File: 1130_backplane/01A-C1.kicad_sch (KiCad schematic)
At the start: 86 parts

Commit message: Finish page RA201-RA271
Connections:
- net -U_BIT_13: now also J254.b9 (Pin_b9)
- net -U_BIT_14: now also J254.a9 (Pin_a9)
- net -U_BIT_15: now also J254.b10 (Pin_b10)
- net -U_BIT_8: now also J254.a5 (Pin_a5)
- net -U_BIT_9: now also J254.b6 (Pin_b6)
- net -U_BIT_10: now reaches J254.a7 (Pin_a7)
- net -U_BIT_12: now reaches J254.a8 (Pin_a8)
- net -U_BIT_11: now reaches J254.b8 (Pin_b8)
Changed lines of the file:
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@@
     (effects (font (size 1.27 1.27)) (justify left bottom))
+  )
+  (label "-U_BIT_10" (at 795.02 157.48 180)
+    (effects (font (size 1.27 1.27)) (justify right bottom))
   )
   (label "KW101_AB4" (at 414.02 297.18 180)
@@
     (effects (font (size 1.27 1.27)) (justify left bottom))
   )
+  (label "-U_BIT_13" (at 807.72 162.56 0)
+    (effects (font (size 1.27 1.27)) (justify left bottom))
+  )
   (label "-3V" (at 596.9 190.5 180)
     (effects (font (size 1.27 1.27)) (justify right bottom))
@@
     (effects (font (size 1.27 1.27)) (justify left bottom))
   )
+  (label "-U_BIT_9" (at 807.72 154.94 0)
+    (effects (font (size 1.27 1.27)) (justify left bottom))
+  )
   (label "+48_VOLTS" (at 223.52 226.06 180)
     (effects (font (size 1.27 1.27)) (justify right bottom))
@@
     (effects (font (size 1.27 1.27)) (justify right bottom))
   )
+  (label "-U_BIT_14" (at 795.02 162.56 180)
+    (effects (font (size 1.27 1.27)) (justify right bottom))
+  )
   (label "+3V" (at 688.34 106.68 0)
     (effects (font (size 1.27 1.27)) (justify left bottom))
@@
     (effects (font (size 1.27 1.27)) (justify right bottom))
   )
+  (label "-U_BIT_8" (at 795.02 152.4 180)
+    (effects (font (size 1.27 1.27)) (justify right bottom))
+  )
   (label "DU101_AU4" (at 414.02 144.78 180)
     (effects (font (size 1.27 1.27)) (justify right bottom))
@@
     (effects (font (size 1.27 1.27)) (justify left bottom))
   )
+  (label "-U_BIT_11" (at 807.72 160.02 0)
+    (effects (font (size 1.27 1.27)) (justify left bottom))
+  )
   (label "-IO_BIT_3" (at 807.72 109.22 0)
     (effects (font (size 1.27 1.27)) (justify left bottom))
@@
     (effects (font (size 1.27 1.27)) (justify left bottom))
   )
+  (label "-U_BIT_15" (at 807.72 165.1 0)
+    (effects (font (size 1.27 1.27)) (justify left bottom))
+  )
   (label "GND" (at 478.79 43.18 90)
     (effects (font (size 1.27 1.27)) (justify left bottom))
@@
     (effects (font (size 1.27 1.27)) (justify right bottom))
   )
+  (label "-U_BIT_12" (at 795.02 160.02 180)
+    (effects (font (size 1.27 1.27)) (justify right bottom))
+  )

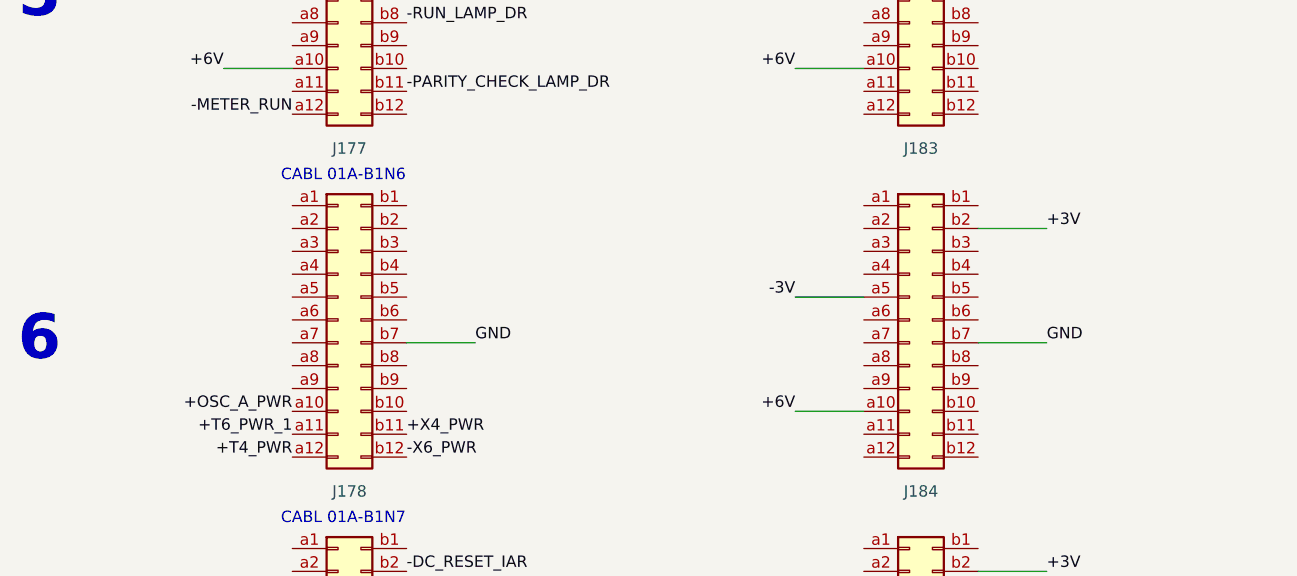
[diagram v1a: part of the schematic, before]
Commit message: Finish page RB301-RB321
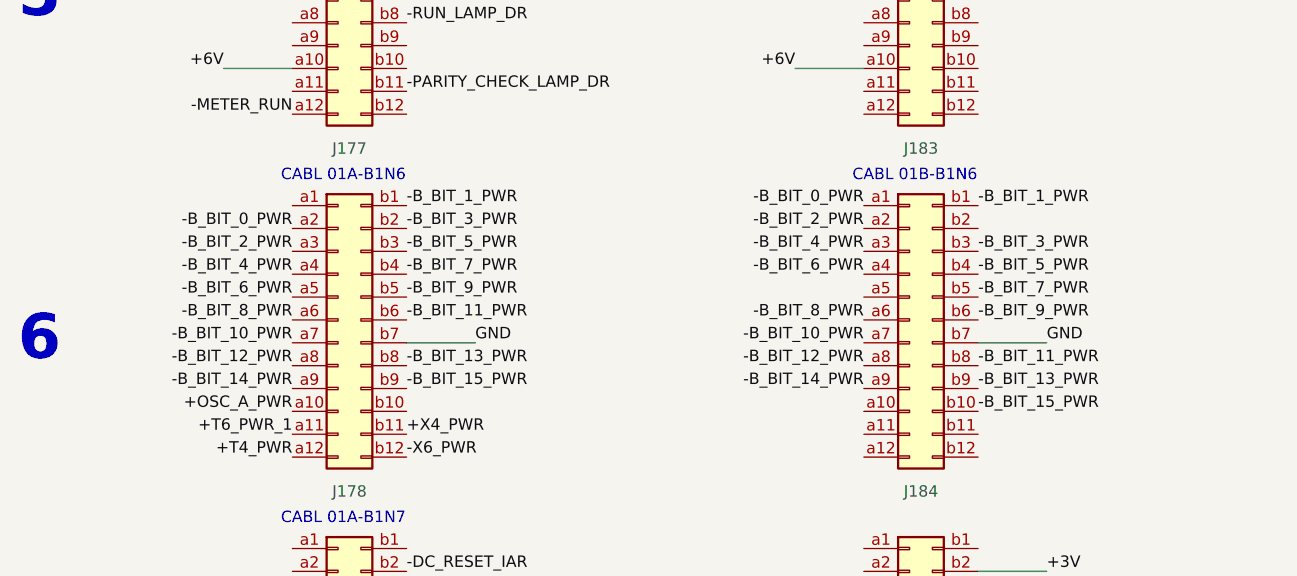
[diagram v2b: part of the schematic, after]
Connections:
- net +3V: no longer J183.b2 (Pin_b2)
- net +6V: no longer J183.a10 (Pin_a10)
- net -3V: no longer J183.a5 (Pin_a5)
- net -B_BIT_0_PWR: now reaches J177.a2 (Pin_a2)
- net -B_BIT_0_PWR: now also J183.a1 (Pin_a1)
- net -B_BIT_2_PWR: now reaches J177.a3 (Pin_a3)
- net -B_BIT_2_PWR: now also J183.a2 (Pin_a2)
- net -B_BIT_4_PWR: now reaches J177.a4 (Pin_a4)
- net -B_BIT_4_PWR: now also J183.a3 (Pin_a3)
- net -B_BIT_6_PWR: now reaches J177.a5 (Pin_a5)
- net -B_BIT_6_PWR: now also J183.a4 (Pin_a4)
- net -B_BIT_8_PWR: now reaches J177.a6 (Pin_a6)
- net -B_BIT_8_PWR: now also J183.a6 (Pin_a6)
- net -B_BIT_10_PWR: now reaches J177.a7 (Pin_a7)
- net -B_BIT_10_PWR: now also J183.a7 (Pin_a7)
- net -B_BIT_12_PWR: now reaches J177.a8 (Pin_a8)
- net -B_BIT_12_PWR: now also J183.a8 (Pin_a8)
- net -B_BIT_14_PWR: now reaches J177.a9 (Pin_a9)
- net -B_BIT_14_PWR: now also J183.a9 (Pin_a9)
- net -B_BIT_1_PWR: now reaches J177.b1 (Pin_b1)
- net -B_BIT_1_PWR: now also J183.b1 (Pin_b1)
- net -B_BIT_3_PWR: now reaches J177.b2 (Pin_b2)
- net -B_BIT_3_PWR: now also J183.b3 (Pin_b3)
- net -B_BIT_5_PWR: now reaches J177.b3 (Pin_b3)
- net -B_BIT_5_PWR: now also J183.b4 (Pin_b4)
- net -B_BIT_7_PWR: now reaches J177.b4 (Pin_b4)
- net -B_BIT_7_PWR: now also J183.b5 (Pin_b5)
- net -B_BIT_9_PWR: now reaches J177.b5 (Pin_b5)
- net -B_BIT_9_PWR: now also J183.b6 (Pin_b6)
- net -B_BIT_11_PWR: now reaches J177.b6 (Pin_b6)
- net -B_BIT_11_PWR: now also J183.b8 (Pin_b8)
- net -B_BIT_13_PWR: now reaches J177.b8 (Pin_b8)
- net -B_BIT_13_PWR: now also J183.b9 (Pin_b9)
- net -B_BIT_15_PWR: now reaches J177.b9 (Pin_b9)
- net -B_BIT_15_PWR: now also J183.b10 (Pin_b10)
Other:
- note added: "CABL 01B-B1N6"
